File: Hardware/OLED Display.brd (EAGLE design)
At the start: 50 x 15 mm, 30 parts, among them J1 QWIIC_RIGHT_ANGLE, J3 QWIIC_RIGHT_ANGLE, U1 QG-2832TLBFG02, U2 APX803

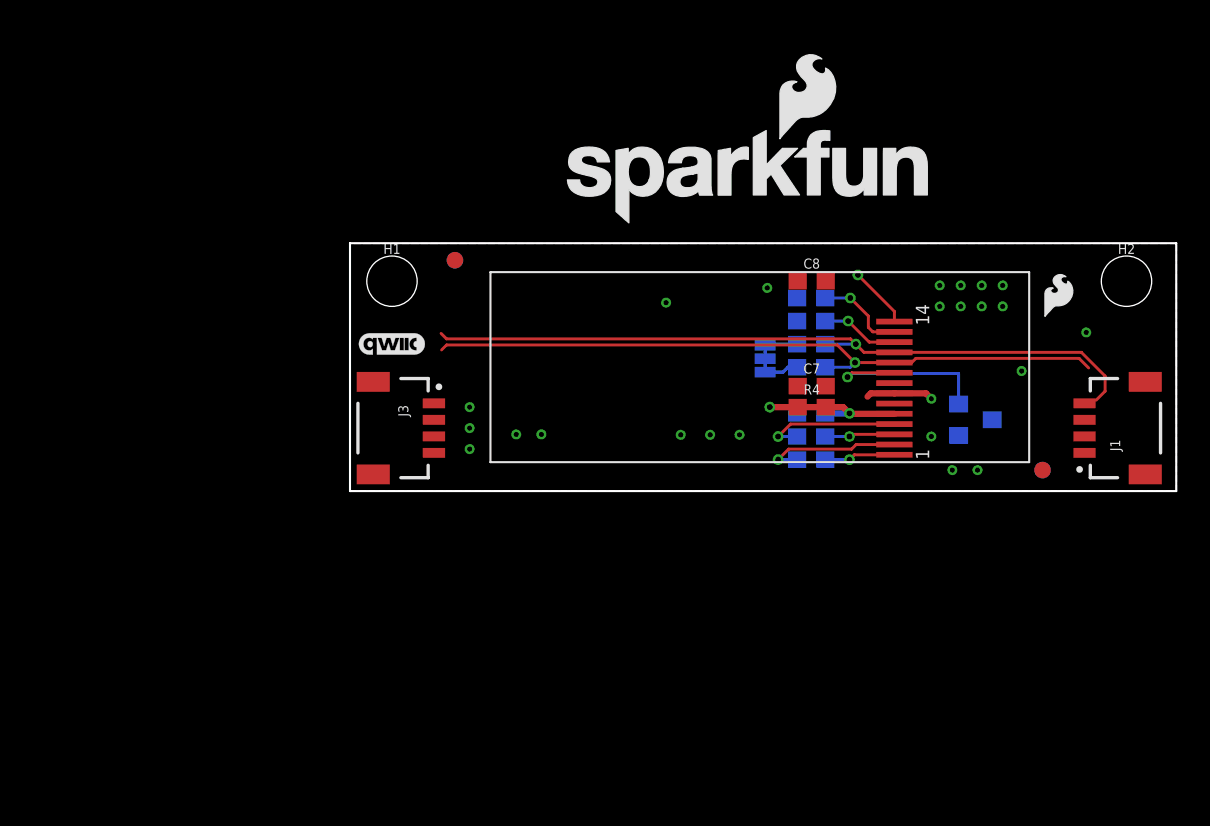
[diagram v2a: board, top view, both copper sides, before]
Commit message: Changes soft start circuit to RC circuit
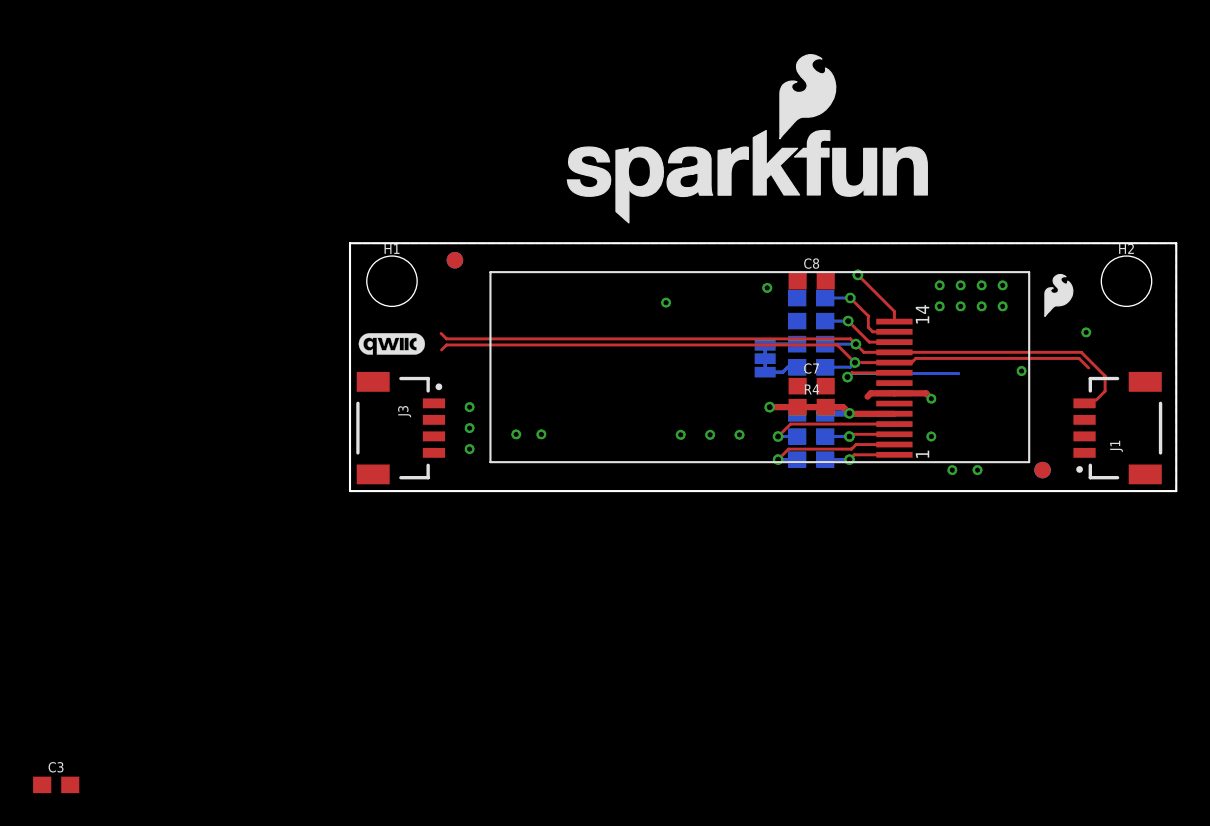
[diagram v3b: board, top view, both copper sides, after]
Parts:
- removed U2: APX803, IC:SOT23
- added C3: 1.0uF, SparkFun-Capacitors:0603
- R1, R2: value 10k -> 4.7k
- R4: value 10k -> 100k
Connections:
- net 3.3V: no longer U2.3
- net GND: now also C3.2; no longer U2.1
- net RST: now also C3.1; no longer U2.2
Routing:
- net RST: track 11.6 -> 9.76 mm
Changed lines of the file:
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@@
 <attribute name="VALUE" value="2.2uF" x="29.305" y="10.2489" size="0.635" layer="28" ratio="10" rot="MR0"/>
 </element>
-<element name="R1" library="SparkFun-Resistors" package="0603" value="10k" x="27.908" y="7.493" smashed="yes" rot="MR0">
+<element name="R1" library="SparkFun-Resistors" package="0603" value="4.7k" x="27.908" y="7.493" smashed="yes" rot="MR0">
 <attribute name="NAME" x="28.67" y="7.112" size="0.8128" layer="26" ratio="10" rot="MR0"/>
 <attribute name="NAME" x="29.178" y="7.239" size="0.635" layer="34" ratio="10" rot="MR0"/>
-<attribute name="PROD_ID" value="RES-00824" x="27.908" y="7.493" size="1.778" layer="28" rot="MR0" display="off"/>
-<attribute name="VALUE" value="10k" x="29.305" y="6.0579" size="0.635" layer="28" ratio="10" rot="MR0"/>
-</element>
-<element name="R2" library="SparkFun-Resistors" package="0603" value="10k" x="27.908" y="8.89" smashed="yes" rot="MR0">
+<attribute name="PROD_ID" value="RES-07857" x="27.908" y="7.493" size="1.778" layer="28" rot="MR0" display="off"/>
+<attribute name="VALUE" value="4.7k" x="29.305" y="6.0579" size="0.635" layer="28" ratio="10" rot="MR0"/>
+</element>
+<element name="R2" library="SparkFun-Resistors" package="0603" value="4.7k" x="27.908" y="8.89" smashed="yes" rot="MR0">
 <attribute name="NAME" x="28.67" y="8.509" size="0.8128" layer="26" ratio="10" rot="MR0"/>
 <attribute name="NAME" x="29.178" y="8.636" size="0.635" layer="34" ratio="10" rot="MR0"/>
-<attribute name="PROD_ID" value="RES-00824" x="27.908" y="8.89" size="1.778" layer="28" rot="MR0" display="off"/>
-<attribute name="VALUE" value="10k" x="29.305" y="7.4549" size="0.635" layer="28" ratio="10" rot="MR0"/>
+<attribute name="PROD_ID" value="RES-07857" x="27.908" y="8.89" size="1.778" layer="28" rot="MR0" display="off"/>
+<attribute name="VALUE" value="4.7k" x="29.305" y="7.4549" size="0.635" layer="28" ratio="10" rot="MR0"/>
 </element>
 <element name="R3" library="SparkFun-Resistors" package="0603" value="470k" x="27.908" y="10.287" smashed="yes" rot="MR180">
@@
 </element>
 <element name="U1" library="Module" package="OLED-12832" value="QG-2832TLBFG02" x="8.5" y="1.75" smashed="yes"/>
-<element name="U2" library="IC" package="SOT23" value="APX803" x="37.846" y="4.318" smashed="yes" rot="MR90">
-<attribute name="NAME" x="39.497" y="2.413" size="0.8128" layer="26" ratio="10" rot="MR90"/>
-<attribute name="VALUE" x="35.433" y="2.413" size="0.8128" layer="28" ratio="10" rot="MR90"/>
-</element>
 <element name="I2C" library="NOA-Jumpers" package="SMT-JUMPER_3_2-NC_TRACE" value="SMT-JUMPER_3_2-NC_TRACE" x="25.1222" y="8.0104" smashed="yes" rot="MR270">
 <attribute name="NAME" x="23.9792" y="8.0104" size="0.6096" layer="26" font="vector" ratio="20" rot="MR270" align="bottom-center"/>
@@
 <attribute name="VALUE" x="47.752" y="2.159" size="0.6096" layer="27" font="vector" ratio="20" rot="R90"/>
 </element>
-<element name="R4" library="SparkFun-Resistors" package="0603" value="10k" x="27.94" y="5.08" smashed="yes">
+<element name="R4" library="SparkFun-Resistors" package="0603" value="100k" x="27.94" y="5.08" smashed="yes">
 <attribute name="NAME" x="27.94" y="5.842" size="0.6096" layer="25" font="vector" ratio="20" align="bottom-center"/>
-<attribute name="PROD_ID" value="RES-00824" x="27.94" y="5.08" size="1.778" layer="27" display="off"/>
-<attribute name="VALUE" x="27.94" y="4.318" size="0.6096" layer="27" font="vector" ratio="20" align="top-center"/>
+<attribute name="PROD_ID" value="RES-07828" x="27.94" y="5.08" size="1.778" layer="27" display="off"/>
+<attribute name="VALUE" value="100k" x="27.94" y="4.318" size="0.6096" layer="27" font="vector" ratio="20" align="top-center"/>
 </element>
 <element name="LOGO4" library="SparkFun-Aesthetics" package="ORDERING_INSTRUCTIONS" value="SPECIAL_INSTRUCTIONS-ORDERING" x="57.404" y="50.673" smashed="yes"/>
+<element name="C3" library="SparkFun-Capacitors" package="0603" value="1.0uF" x="-17.78" y="-17.78" smashed="yes">
+<attribute name="NAME" x="-17.78" y="-17.018" size="0.6096" layer="25" font="vector" ratio="20" align="bottom-center"/>
+<attribute name="PROD_ID" value="CAP-00868" x="-17.78" y="-17.78" size="1.778" layer="27" font="vector" ratio="15" display="off"/>
+<attribute name="VALUE" x="-17.78" y="-18.542" size="0.6096" layer="27" font="vector" ratio="20" align="top-center"/>
+</element>
 </elements>
 <signals>
@@
 <contactref element="J1" pad="1"/>
 <contactref element="J3" pad="1"/>
-<contactref element="U2" pad="1"/>
 <contactref element="U1" pad="7"/>
 <via x="35.179" y="5.588" extent="1-16" drill="0.3048"/>
@@
 <wire x1="32.945" y1="5.915" x2="31.5182" y2="5.915" width="0.381" layer="1"/>
 <wire x1="31.5182" y1="5.915" x2="31.3182" y2="5.715" width="0.381" layer="1"/>
+<contactref element="C3" pad="2"/>
 <wire x1="40.64" y1="7.2644" x2="44.5516" y2="9.6012" width="0" layer="19" extent="1-1"/>
 <wire x1="39.497" y1="11.176" x2="40.64" y2="7.2644" width="0" layer="19" extent="1-1"/>
@@
 <wire x1="36.957" y1="11.176" x2="38.227" y2="11.176" width="0" layer="19" extent="1-1"/>
 <wire x1="35.687" y1="11.176" x2="35.687" y2="12.446" width="0" layer="19" extent="1-1"/>
-<wire x1="36.83" y1="3.368" x2="40.64" y2="7.2644" width="0" layer="19" extent="16-16"/>
-<wire x1="35.179" y1="3.302" x2="36.83" y2="3.368" width="0" layer="19" extent="16-16"/>
-<wire x1="36.449" y1="1.27" x2="36.83" y2="3.368" width="0" layer="19" extent="16-16"/>
+<wire x1="35.179" y1="5.588" x2="35.687" y2="11.176" width="0" layer="19" extent="1-1"/>
+<wire x1="35.179" y1="3.302" x2="35.179" y2="5.588" width="0" layer="19" extent="1-1"/>
+<wire x1="36.449" y1="1.27" x2="35.179" y2="3.302" width="0" layer="19" extent="1-1"/>
 <wire x1="37.973" y1="1.27" x2="36.449" y2="1.27" width="0" layer="19" extent="1-1"/>
-<wire x1="35.179" y1="5.588" x2="35.179" y2="3.302" width="0" layer="19" extent="1-1"/>
 <wire x1="27.09" y1="6.35" x2="31.3182" y2="5.715" width="0" layer="19" extent="1-1"/>
 <wire x1="27.058" y1="4.699" x2="27.09" y2="6.35" width="0" layer="19" extent="1-16"/>
@@
 <wire x1="7.239" y1="2.54" x2="7.239" y2="3.81" width="0" layer="19" extent="1-1"/>
 <wire x1="5.08" y1="5.31" x2="7.239" y2="5.08" width="0" layer="19" extent="1-1"/>
+<wire x1="-16.93" y1="-17.78" x2="7.239" y2="2.54" width="0" layer="19" extent="1-1"/>
 </signal>
 <signal name="SCL">
@@
 <signal name="RST">
 <contactref element="U1" pad="9"/>
-<contactref element="U2" pad="2"/>
 <wire x1="32.945" y1="7.155" x2="30.361525" y2="7.155" width="0.1778" layer="1"/>
 <wire x1="30.361525" y1="7.155" x2="30.10541875" y2="6.89889375" width="0.1778" layer="1"/>
@@
 <wire x1="36.8214125" y1="7.112" x2="30.318525" y2="7.112" width="0.1778" layer="16"/>
 <wire x1="30.318525" y1="7.112" x2="30.10541875" y2="6.89889375" width="0.1778" layer="16"/>
-<wire x1="36.83" y1="5.268" x2="36.83" y2="7.1034125" width="0.1778" layer="16"/>
 <wire x1="36.83" y1="7.1034125" x2="36.8214125" y2="7.112" width="0.1778" layer="16"/>
 <contactref element="R4" pad="1"/>
+<contactref element="C3" pad="1"/>
+<wire x1="27.09" y1="5.08" x2="-18.63" y2="-17.78" width="0" layer="19" extent="1-1"/>
 <wire x1="30.10541875" y1="6.89889375" x2="27.09" y2="5.08" width="0" layer="19" extent="1-1"/>
 </signal>
@@
 <contactref element="J1" pad="2"/>
 <contactref element="I2C" pad="2"/>
-<contactref element="U2" pad="3"/>
 <contactref element="R4" pad="2"/>
-<wire x1="44.45" y1="3.31" x2="28.79" y2="5.08" width="0" layer="19" extent="1-1"/>
-<wire x1="5.08" y1="4.31" x2="44.45" y2="3.31" width="0" layer="19" extent="1-1"/>
-<wire x1="28.79" y1="12.7" x2="5.08" y2="4.31" width="0" layer="19" extent="1-1"/>
-<wire x1="25.4" y1="5.08" x2="28.79" y2="12.7" width="0" layer="19" extent="1-1"/>
+<wire x1="32.945" y1="4.675" x2="44.45" y2="3.31" width="0" layer="19" extent="1-1"/>
+<wire x1="28.79" y1="5.08" x2="28.758" y2="4.699" width="0" layer="19" extent="1-16"/>
 <wire x1="32.945" y1="6.535" x2="32.945" y2="4.675" width="0" layer="19" extent="1-1"/>
 <wire x1="25.1222" y1="8.0104" x2="25.4" y2="5.08" width="0" layer="19" extent="16-16"/>
-<wire x1="38.862" y1="4.318" x2="32.945" y2="4.675" width="0" layer="19" extent="1-16"/>
+<wire x1="28.79" y1="12.7" x2="25.1222" y2="8.0104" width="0" layer="19" extent="1-16"/>
+<wire x1="5.08" y1="4.31" x2="25.4" y2="5.08" width="0" layer="19" extent="1-1"/>
 </signal>
 </signals>

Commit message: Shrinks the overall size of the board
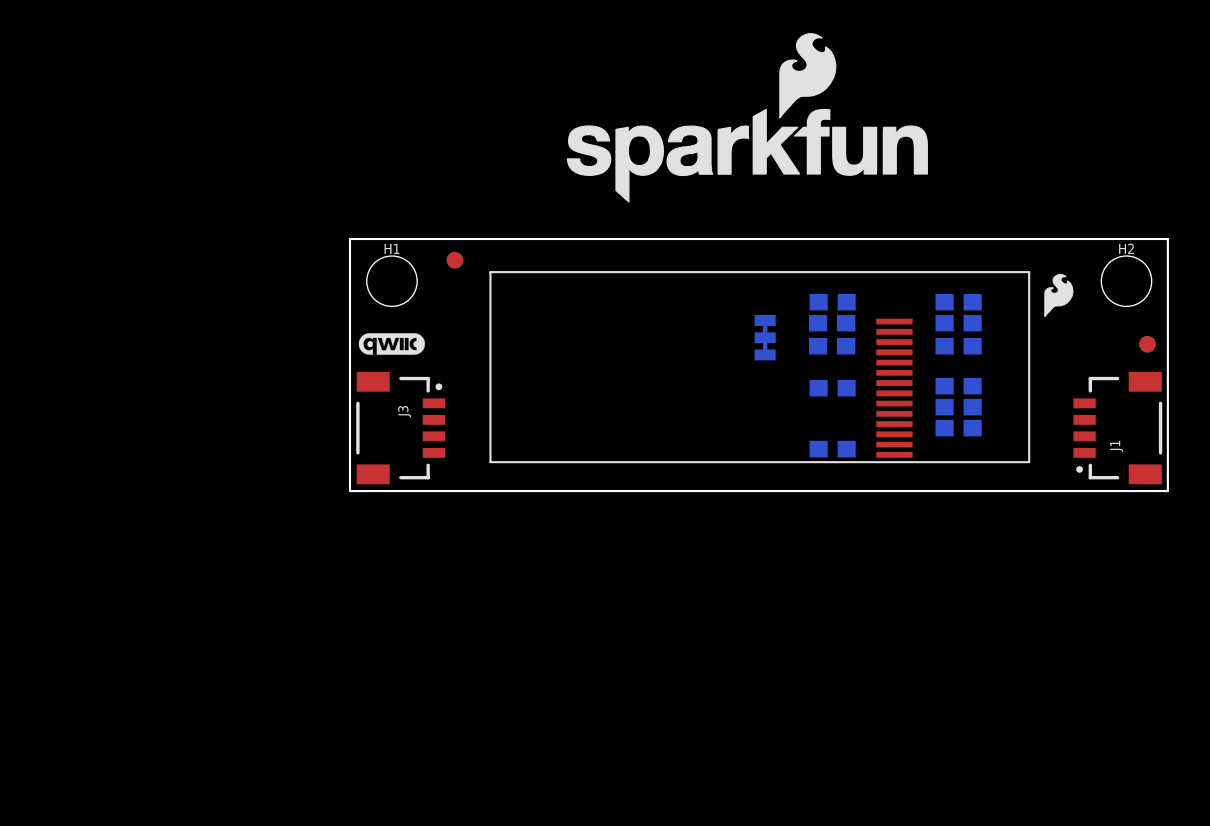
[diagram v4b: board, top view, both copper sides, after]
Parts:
- removed U$20: (no value), Labels:I_SUPER2_C-()-04
- I2C: value SMT-JUMPER_3_2-NC_TRACE -> JUMPER-SMT_3_2-NC_TRACE_SILK; device NOA-Jumpers:SMT-JUMPER_3_2-NC_TRACE -> SparkFun-Jumpers:SMT-JUMPER_3_2-NC_TRACE_SILK
- moved C3 52.8 mm to (29.2, 6.22), flipped to the bottom
- moved C8 11.7 mm to (36.8, 5.08), flipped to the bottom
- moved C7 10.2 mm to (36.8, 11.4), flipped to the bottom
- moved FD3 9.92 mm to (48.3, 8.89)
- moved FD4 9.92 mm to (48.3, 8.89)
- moved R4 9.62 mm to (36.8, 8.76), flipped to the bottom, turned to 180 degrees
- moved C4 9.07 mm to (36.8, 6.35), turned to 180 degrees
- moved C2 8.94 mm to (36.8, 3.81), turned to 0 degrees
- moved R3 8.92 mm to (36.8, 10.2), turned to 0 degrees
- moved R1 1.80 mm to (29.2, 8.76)
- moved R2 1.80 mm to (29.2, 10.2)
- moved C1 1.45 mm to (29.2, 2.54)
- moved C5 1.33 mm to (29.2, 11.4)
- moved I2C 1.27 mm to (25.1, 9.28)
- moved LOGO1 1.27 mm to (24.1, 20.3)
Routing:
- net SDA: track 44.8 -> 0.00 mm, vias 1 -> 0
- net SCL: track 42.0 -> 0.00 mm, vias 1 -> 0
- net RST: track 9.76 -> 0.00 mm, vias 1 -> 0
- net 3.3V: track 9.18 -> 0.00 mm, vias 2 -> 0
- net N$2: track 8.56 -> 0.00 mm, vias 1 -> 0
- net N$4: track 8.50 -> 0.00 mm, vias 1 -> 0
- net N$6: track 5.44 -> 0.00 mm, vias 1 -> 0
- net N$9: track 4.71 -> 0.00 mm, vias 1 -> 0
- net N$1: track 4.31 -> 0.00 mm, vias 1 -> 0
- net N$3: track 4.24 -> 0.00 mm, vias 1 -> 0
- net GND: track 4.08 -> 0.00 mm, vias 24 -> 0
- net N$7: track 3.74 -> 0.00 mm, vias 1 -> 0
- net N$5: track 2.06 -> 0.00 mm
- net N$8: track 1.96 -> 0.00 mm
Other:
- board size 50 x 15 mm -> 49.5 x 15.3 mm
- board text added: "NOA Labs"
- board text added: "Revised By: Elias Santistevan"
- board text removed: "1"
- board text removed: "14"

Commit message: Routes the board
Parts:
- removed C3: 1.0uF, SparkFun-Capacitors:0603
- removed U$7: (no value), buzzard_labels:0#91_IN#_OLED_V1#0_128X320
- removed U$8: (no value), SparkFun-Aesthetics_Font_Logo:SFE_LOGO_FLAME_.1
- removed U$9: (no value), SparkFun-Aesthetics_Flame_Logo:SFE_LOGO_NAME_FLAME_.1
- removed U1: QG-2832TLBFG02, Module:OLED-12832
- added U$1: (no value), SparkFun-Aesthetics:SFE_LOGO_FLAME_.2
- added U2: APX803S-SA, Module:SOT23-3
- added U3: OLED_0.9"-QG-2832TLBFG02, Module:OLED-12832
- LOGO1: value SFE_LOGO_NAME_FLAME.2_INCH -> SFE_LOGO_NAME_FLAME.1_INCH; device SparkFun-Aesthetics:SFE_LOGO_NAME_FLAME_.2 -> SparkFun-Aesthetics:SFE_LOGO_NAME_FLAME_.1
- R4: value 100k -> 10k
- moved LOGO1 20.5 mm to (14.0, 2.54), flipped to the bottom
- moved FD1 12.8 mm to (7.62, 1.27)
- moved FD2 12.8 mm to (7.62, 1.27)
- moved LOGO2 10.6 mm to (3.61, 1.98), flipped to the top
- moved FD3 10.5 mm to (38.1, 11.4)
- moved FD4 10.5 mm to (38.1, 11.4)
- moved I2C 6.81 mm to (30.5, 5.08), turned to 0 degrees
- moved LOGO3 6.59 mm to (6.73, 3.81), flipped to the bottom, turned to 90 degrees
- moved H2 5.68 mm to (41.9, 10.2)
- moved J1 5.08 mm to (39.4, 3.81), flipped to the bottom, turned to 270 degrees
- moved C2 3.59 mm to (34.3, 1.27)
- moved C8 3.59 mm to (34.3, 2.54)
- moved R3 3.59 mm to (34.3, 7.62)
- moved R4 3.59 mm to (34.3, 6.22)
- moved C4 3.59 mm to (34.3, 3.81)
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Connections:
- removed net N$3: C2.2, U1.3
- new net N$17: C2.1, U3.2
- net 3.3V: now also U2.3, U3.5, U3.8; no longer U1.5, U1.8
- net GND: now also U2.1, U3.7; no longer C3.2, U1.7
- net N$1: now also C2.2, U3.1; no longer C1.2, U1.1
- net N$2: now also U3.4; no longer U1.2
- net N$4: now also C1.2, U3.3; no longer C2.1, U1.4
- net N$6: now also U3.13; no longer U1.13
- net N$7: now also U3.14; no longer U1.14
- net N$9: now also U3.12; no longer U1.12
- net RST: now also U2.2, U3.9; no longer C3.1, U1.9
- net SCL: now also U3.10; no longer U1.10
- net SDA: now also U3.11; no longer U1.11
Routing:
- net SDA: track 0.00 -> 50.4 mm, vias 0 -> 2
- net 3.3V: track 0.00 -> 41.0 mm, vias 0 -> 1
- net SCL: track 0.00 -> 40.6 mm, vias 0 -> 2
- net N$17: track 0.00 -> 9.25 mm, vias 0 -> 1
- net N$8: track 0.00 -> 8.50 mm
- net N$2: track 0.00 -> 7.50 mm, vias 0 -> 1
- net RST: track 0.00 -> 6.96 mm, vias 0 -> 2
- net N$5: track 0.00 -> 4.02 mm
- net N$4: track 0.00 -> 3.88 mm, vias 0 -> 1
- net N$7: track 0.00 -> 3.39 mm, vias 0 -> 1
- net N$9: track 0.00 -> 3.25 mm, vias 0 -> 1
- net N$1: track 0.00 -> 3.10 mm, vias 0 -> 1
- net N$6: track 0.00 -> 2.94 mm, vias 0 -> 1
- added copper zone on layer 1, net 3.3V
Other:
- board size 49.5 x 15.3 mm -> 44.4 x 12.7 mm
- board text added: "Units in Inches"
